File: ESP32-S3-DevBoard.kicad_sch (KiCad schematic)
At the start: 15 parts, among them J1 USB_C_Receptacle_USB2.0_14P, SW1 SW_Push, U1 ESP32-S3-WROOM-1, U2 AMS1117-3.3

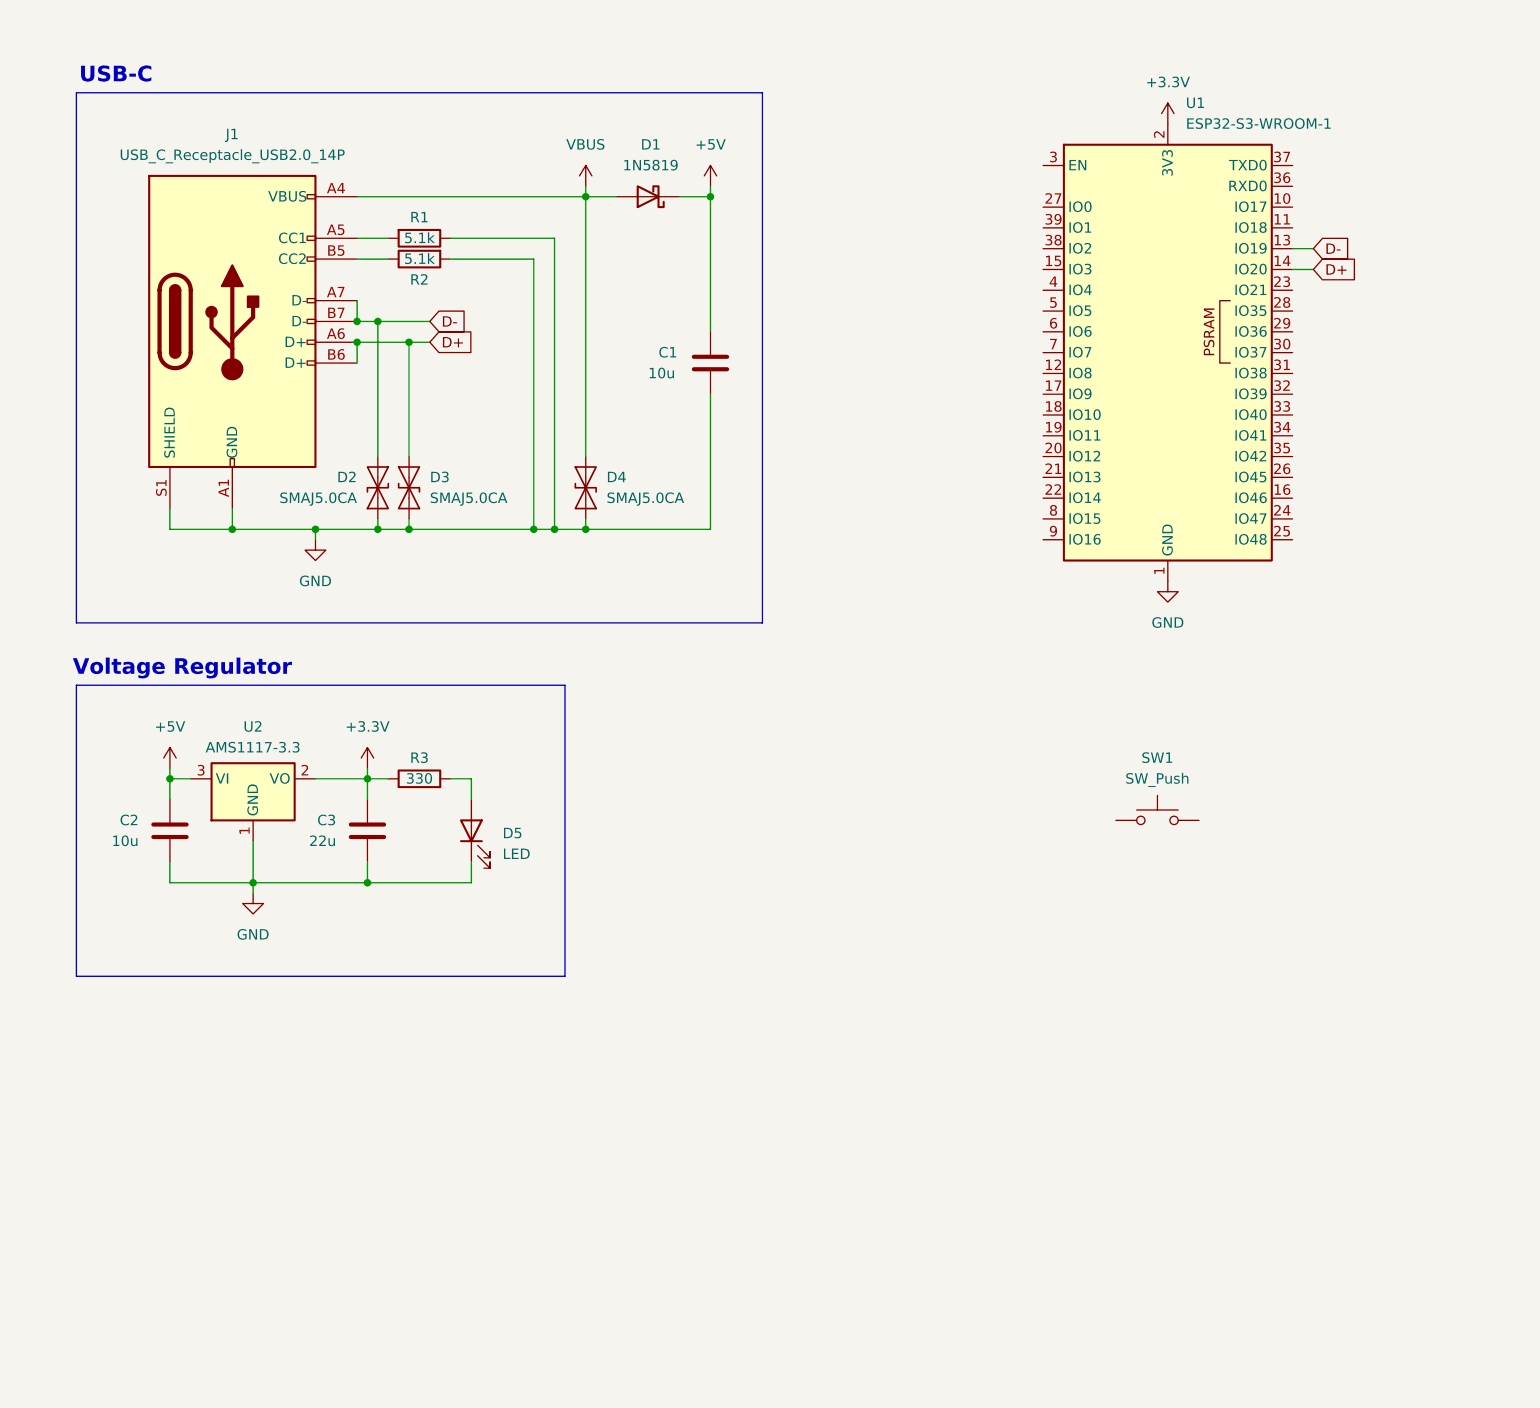
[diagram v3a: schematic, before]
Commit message: Add buttons and decoupled 3.3V
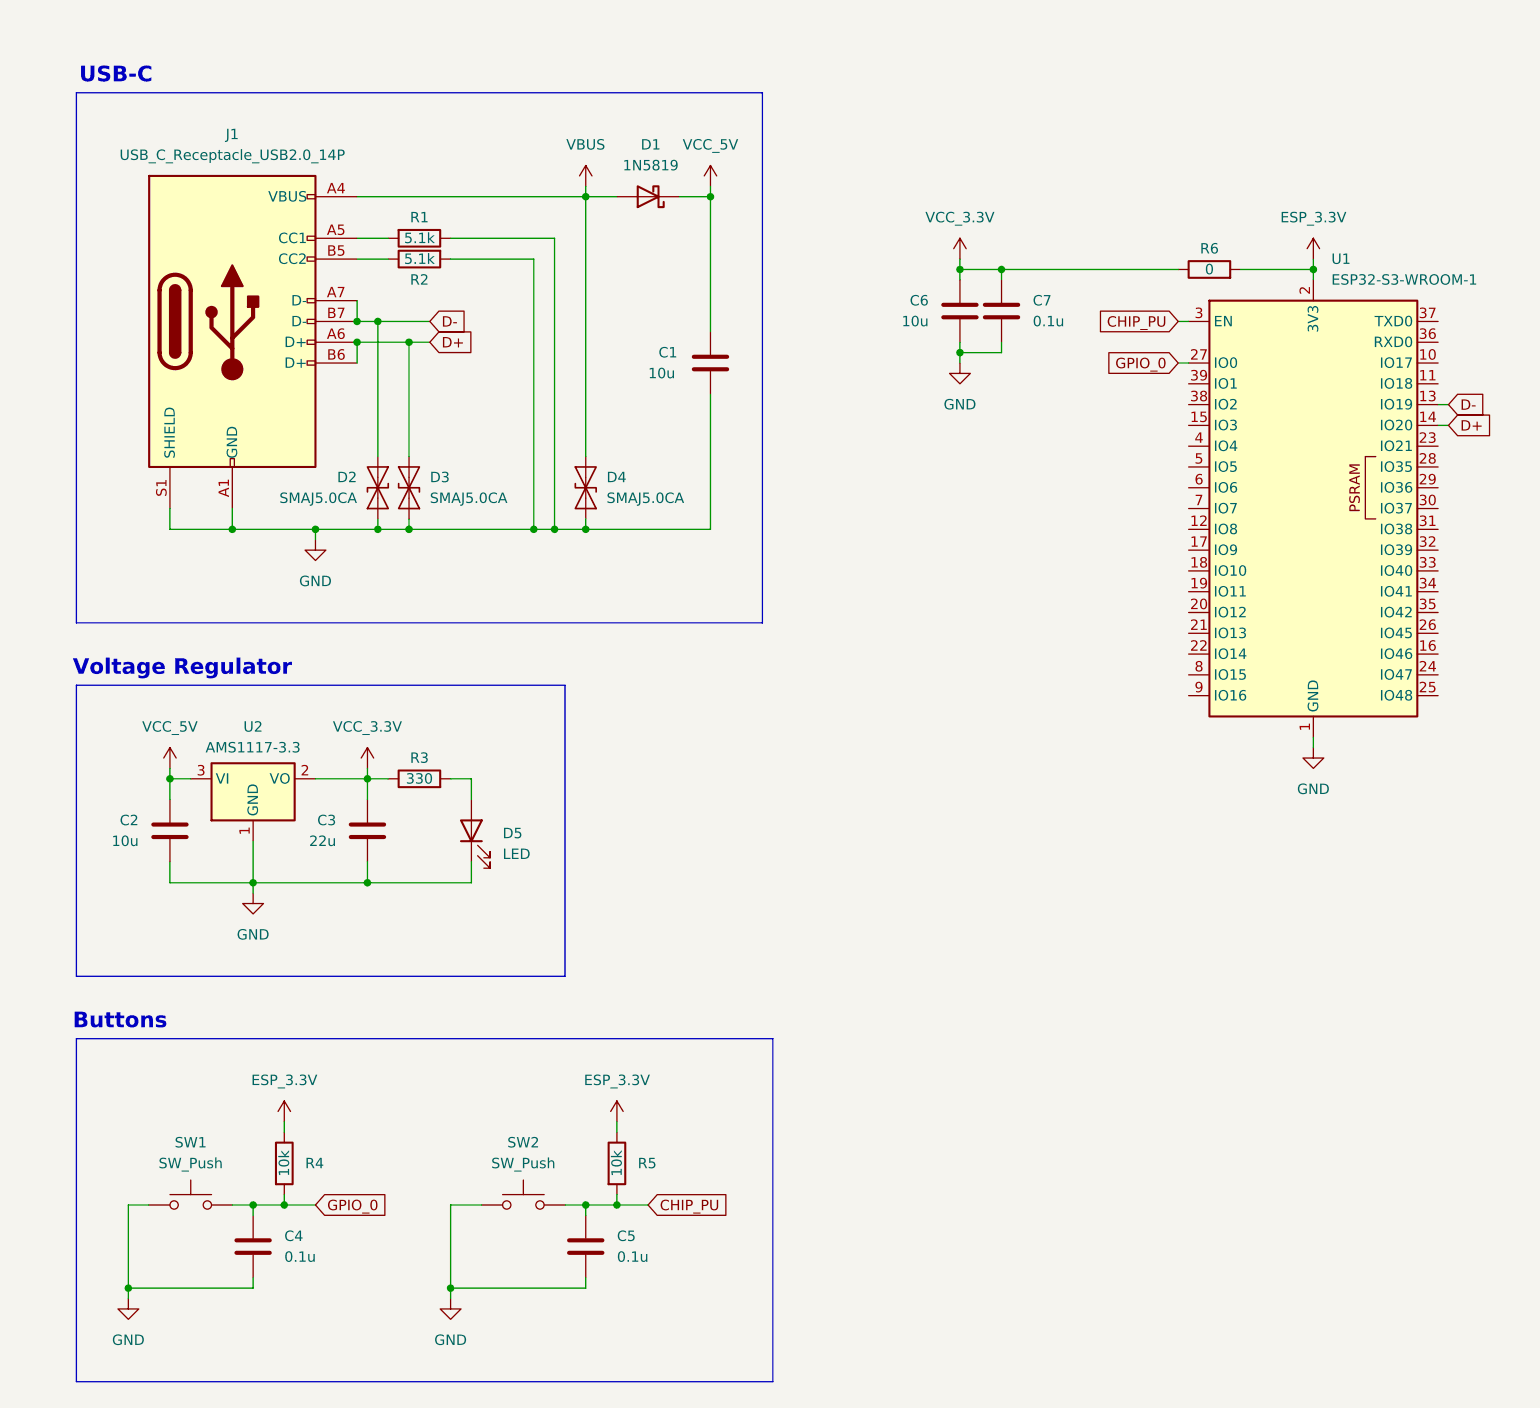
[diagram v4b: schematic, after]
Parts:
- added C4, C5, C7: 0.1u, symbol Device:C
- added C6: 10u, symbol Device:C
- added R4, R5: 10k, symbol Device:R
- added R6: 0, symbol Device:R
- added SW2: SW_Push, symbol Switch:SW_Push
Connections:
- net GND: now also SW1.1, C4.2, C5.2, C6.2, C7.2, SW2.1
- net GPIO_0: now reaches SW1.2
- net GPIO_0: now also U1.27 (IO0), C4.1, R4.2
- net CHIP_PU: now reaches U1.3 (EN)
- net CHIP_PU: now also C5.1, R5.2, SW2.2
- net +3.3V renamed VCC_3.3V
- net VCC_3.3V: now also C6.1, C7.1, R6.1; no longer U1.2 (3V3)
- net +5V renamed VCC_5V
- new net ESP_3.3V: R4.1, R5.1, R6.2, U1.2 (3V3)
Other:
- note added: "Buttons"
- moved on the sheet: U1

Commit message: Decouple remaining power supplies
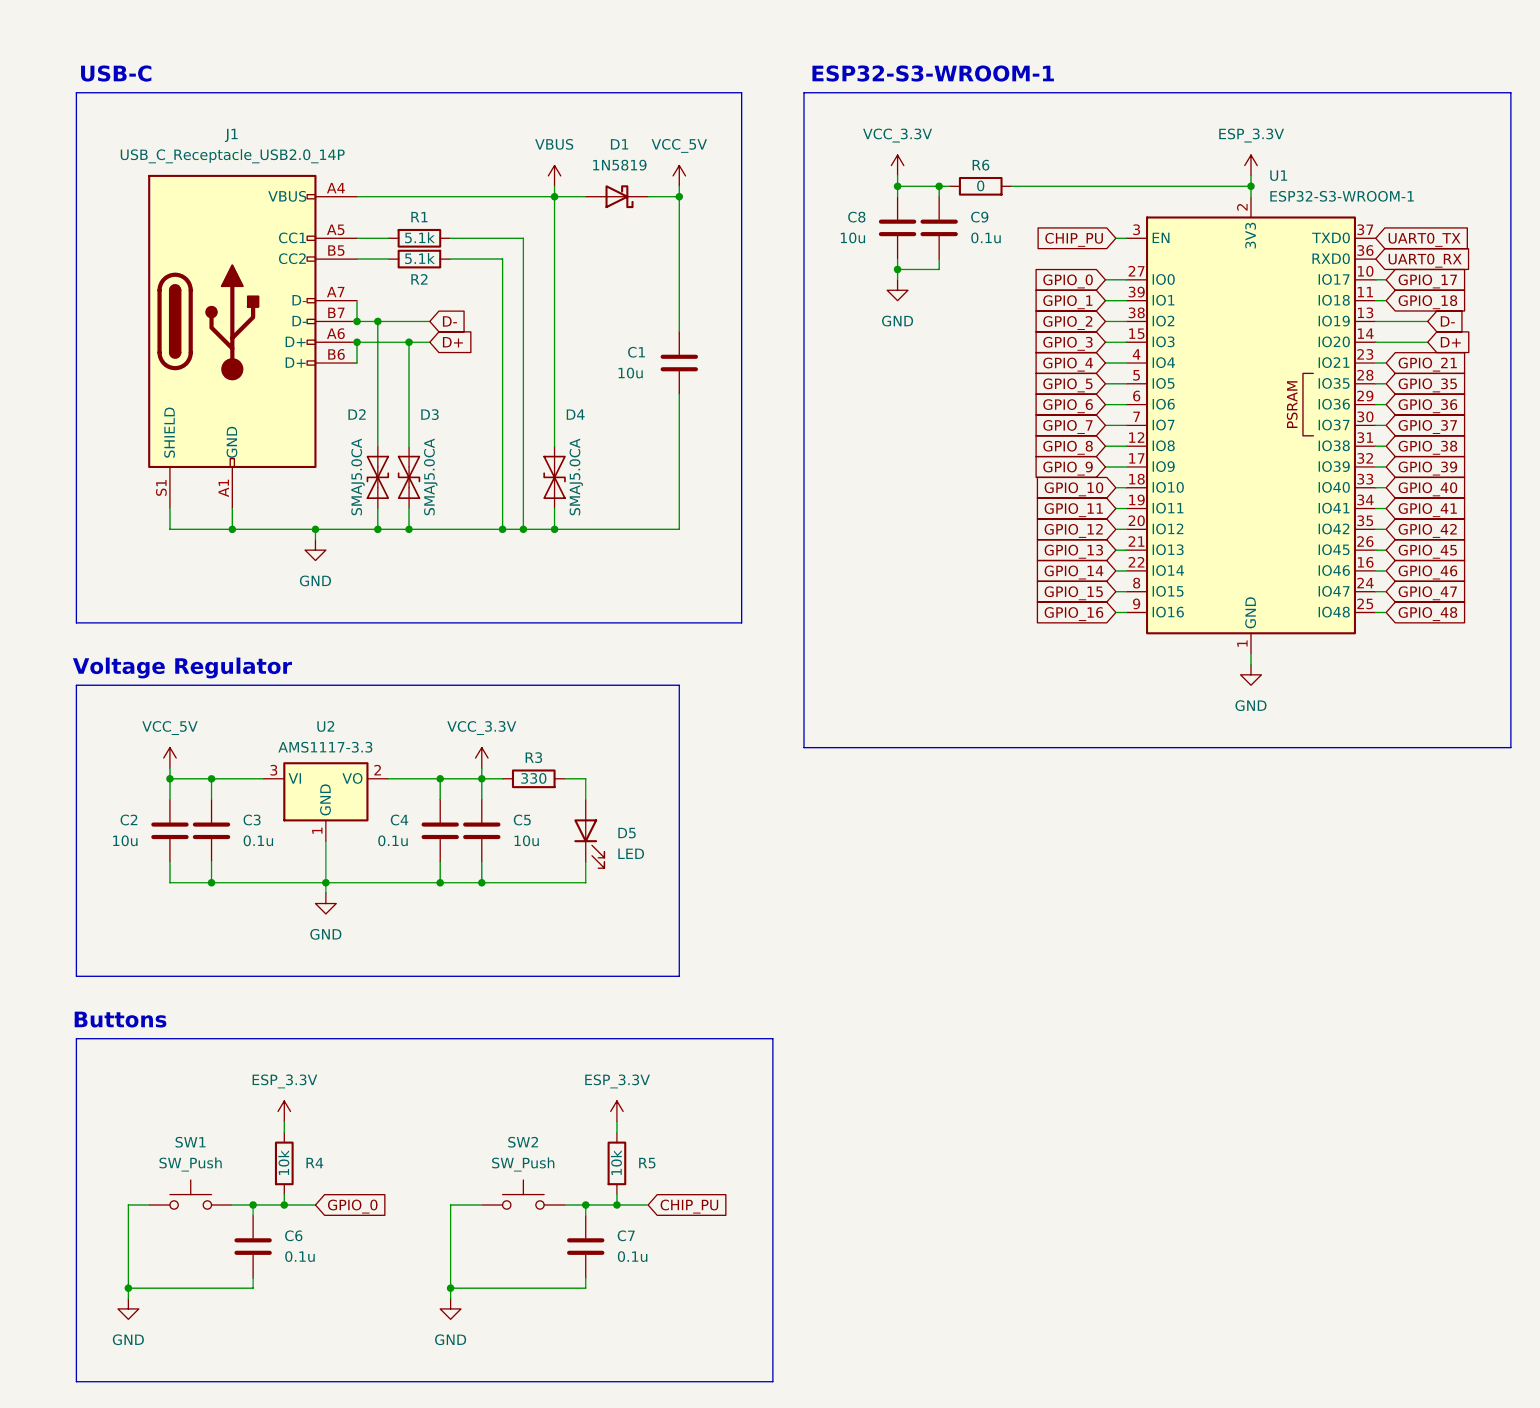
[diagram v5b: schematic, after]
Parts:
- added C2, C5: 10u, symbol Device:C
- C3: renamed from C2; value 10u -> 0.1u
- C4: renamed from C3; value 22u -> 0.1u
- renumbered C4 to C6, C5 to C7, C6 to C8, C7 to C9
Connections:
- net GND: now also C2.2, C5.2
- net VCC_3.3V: now also C5.1
- net VCC_5V: now also C2.1
- net GPIO_17: now reaches U1.10 (IO17)
- net GPIO_18: now reaches U1.11 (IO18)
- net GPIO_8: now reaches U1.12 (IO8)
- net GPIO_3: now reaches U1.15 (IO3)
- net GPIO_46: now reaches U1.16 (IO46)
- net GPIO_9: now reaches U1.17 (IO9)
- net GPIO_10: now reaches U1.18 (IO10)
- net GPIO_11: now reaches U1.19 (IO11)
- net GPIO_12: now reaches U1.20 (IO12)
- net GPIO_13: now reaches U1.21 (IO13)
- net GPIO_14: now reaches U1.22 (IO14)
- net GPIO_21: now reaches U1.23 (IO21)
- net GPIO_47: now reaches U1.24 (IO47)
- net GPIO_48: now reaches U1.25 (IO48)
- net GPIO_45: now reaches U1.26 (IO45)
- net GPIO_35: now reaches U1.28 (IO35)
- net GPIO_36: now reaches U1.29 (IO36)
- net GPIO_37: now reaches U1.30 (IO37)
- net GPIO_38: now reaches U1.31 (IO38)
- net GPIO_39: now reaches U1.32 (IO39)
- net GPIO_40: now reaches U1.33 (IO40)
- net GPIO_41: now reaches U1.34 (IO41)
- net GPIO_42: now reaches U1.35 (IO42)
- net UART0_RX: now reaches U1.36 (RXD0)
- net UART0_TX: now reaches U1.37 (TXD0)
- net GPIO_2: now reaches U1.38 (IO2)
- net GPIO_1: now reaches U1.39 (IO1)
- net GPIO_4: now reaches U1.4 (IO4)
- net GPIO_5: now reaches U1.5 (IO5)
- net GPIO_6: now reaches U1.6 (IO6)
- net GPIO_7: now reaches U1.7 (IO7)
- net GPIO_15: now reaches U1.8 (IO15)
- net GPIO_16: now reaches U1.9 (IO16)
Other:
- note added: "ESP32-S3-WROOM-1"
- moved on the sheet: C1, C3, C4, C8, C9, D1, D2, D3, D4, D5, R6, U1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

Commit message: Breakout pins to headers
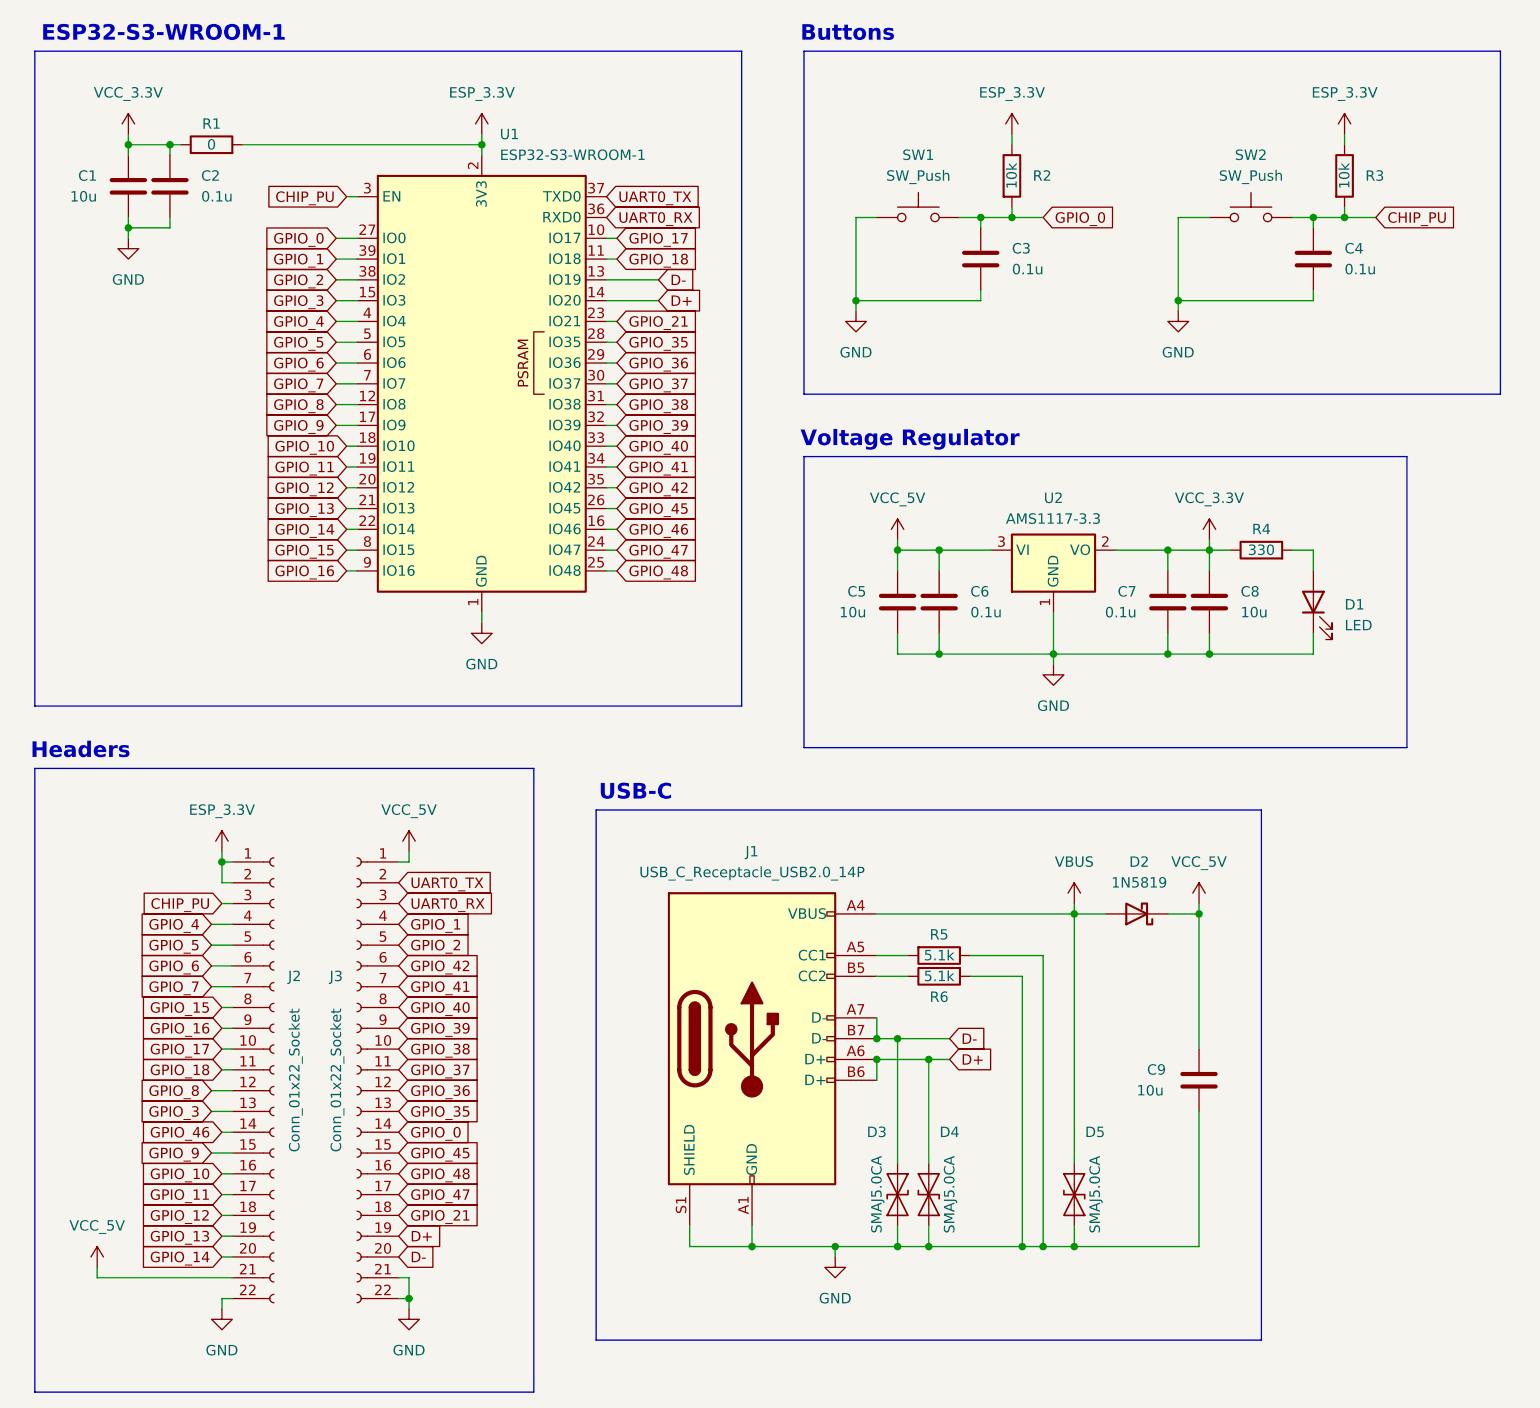
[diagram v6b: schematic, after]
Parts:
- added J2, J3: Conn_01x22_Socket, symbol Connector:Conn_01x22_Socket
- renumbered C8 to C1, C9 to C2, C6 to C3, C7 to C4, C2 to C5, C3 to C6, C4 to C7, C5 to C8, C1 to C9, D5 to D1, D1 to D2, D2 to D3, D3 to D4, D4 to D5, R6 to R1, R4 to R2, R5 to R3, R3 to R4, R1 to R5, R2 to R6
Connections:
- net CHIP_PU: now also J2.3 (Pin_3)
- net D+: now also J3.19 (Pin_19)
- net D-: now also J3.20 (Pin_20)
- net ESP_3.3V: now also J2.1 (Pin_1), J2.2 (Pin_2)
- net GND: now also J2.22 (Pin_22), J3.21 (Pin_21), J3.22 (Pin_22)
- net GPIO_0: now also J3.14 (Pin_14)
- net GPIO_1: now also J3.4 (Pin_4)
- net GPIO_10: now also J2.16 (Pin_16)
- net GPIO_11: now also J2.17 (Pin_17)
- net GPIO_12: now also J2.18 (Pin_18)
- net GPIO_13: now also J2.19 (Pin_19)
- net GPIO_14: now also J2.20 (Pin_20)
- net GPIO_15: now also J2.8 (Pin_8)
- net GPIO_16: now also J2.9 (Pin_9)
- net GPIO_17: now also J2.10 (Pin_10)
- net GPIO_18: now also J2.11 (Pin_11)
- net GPIO_2: now also J3.5 (Pin_5)
- net GPIO_21: now also J3.18 (Pin_18)
- net GPIO_3: now also J2.13 (Pin_13)
- net GPIO_35: now also J3.13 (Pin_13)
- net GPIO_36: now also J3.12 (Pin_12)
- net GPIO_37: now also J3.11 (Pin_11)
- net GPIO_38: now also J3.10 (Pin_10)
- net GPIO_39: now also J3.9 (Pin_9)
- net GPIO_4: now also J2.4 (Pin_4)
- net GPIO_40: now also J3.8 (Pin_8)
- net GPIO_41: now also J3.7 (Pin_7)
- net GPIO_42: now also J3.6 (Pin_6)
- net GPIO_45: now also J3.15 (Pin_15)
- net GPIO_46: now also J2.14 (Pin_14)
- net GPIO_47: now also J3.17 (Pin_17)
- net GPIO_48: now also J3.16 (Pin_16)
- net GPIO_5: now also J2.5 (Pin_5)
- net GPIO_6: now also J2.6 (Pin_6)
- net GPIO_7: now also J2.7 (Pin_7)
- net GPIO_8: now also J2.12 (Pin_12)
- net GPIO_9: now also J2.15 (Pin_15)
- net UART0_RX: now also J3.3 (Pin_3)
- net UART0_TX: now also J3.2 (Pin_2)
- net VCC_5V: now also J2.21 (Pin_21), J3.1 (Pin_1)
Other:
- note added: "Headers"
- moved on the sheet: C1, C2, C3, C4, C5, C6, C7, C8, C9, D1, D2, D3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
